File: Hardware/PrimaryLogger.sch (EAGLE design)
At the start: 72 parts, among them J1 CONN_42.54_SCREW, J2 CONN_42.54_SCREW, J3 CONN_42.54_SCREW, J4 CONN_42.54_SCREW, J5 CONN_32.54_SCREW, Q1 DMG3404, Q2 DMG3404, U1 MIC2005, U2 MIC2005, U25 SN74AUP3G34DCU, U3 TPL5010DDC, U4 TXS0102DCU, U5 SN74LVC1G3157SC70, U6 TCS3400, U7 SHTC3DFN, U8 MCP23008QFN, U9 MCP7940SOIC

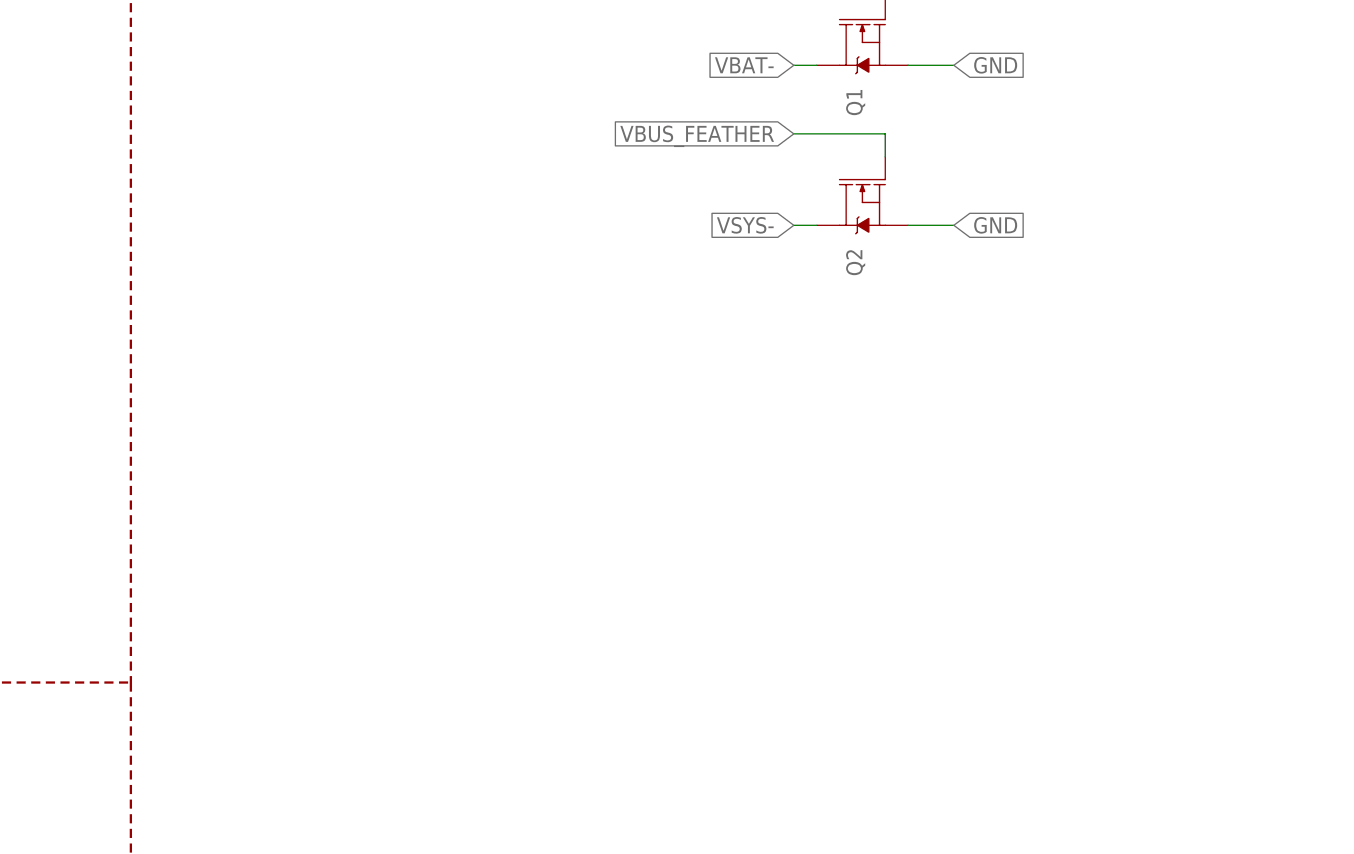
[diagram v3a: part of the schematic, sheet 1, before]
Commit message: Added LED support for v0.3
Schematic capture and preliminary layout of LED indicator
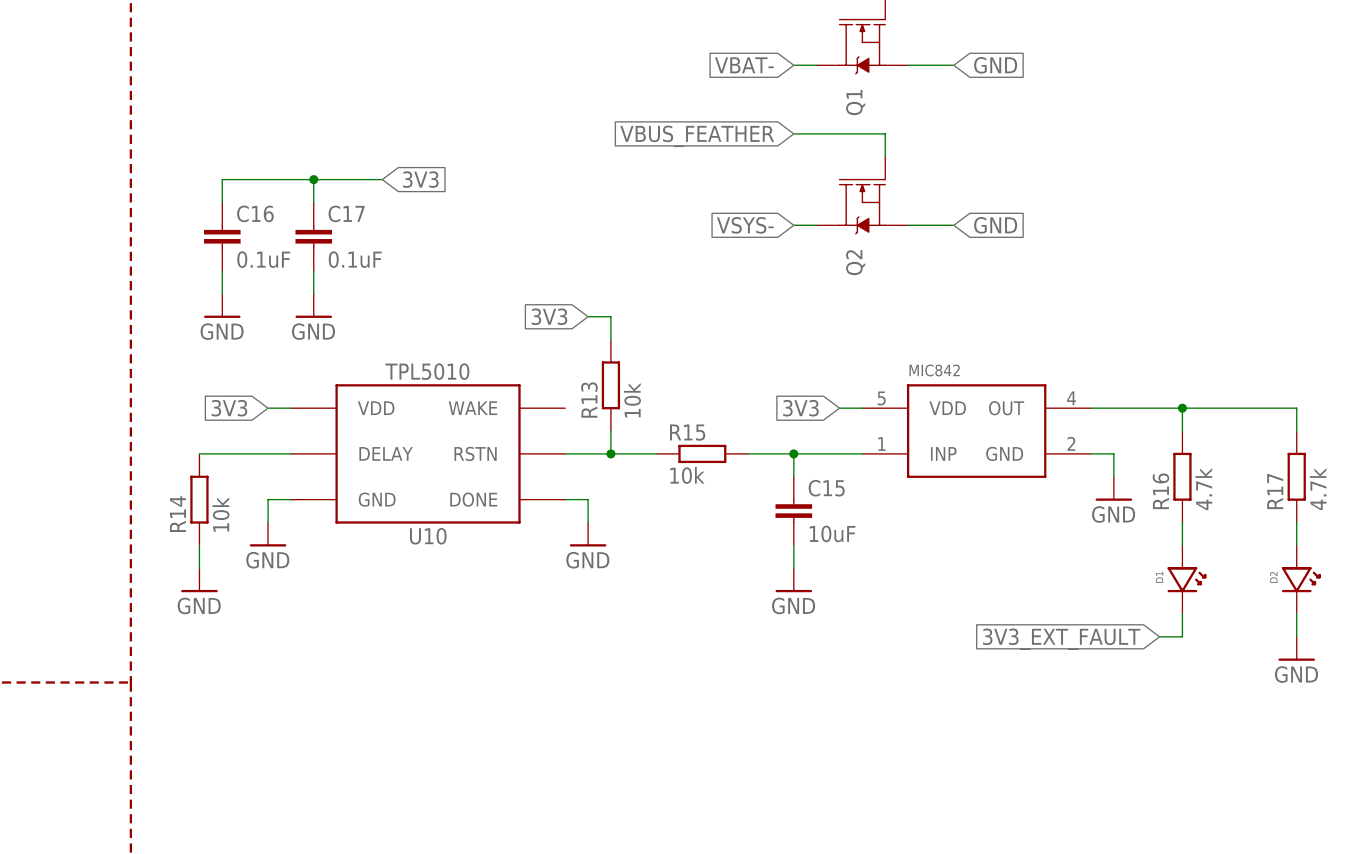
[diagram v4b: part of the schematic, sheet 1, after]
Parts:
- added C15: 10uF, bschulz_passives:C-EU10UFC0805
- added C16, C17: 0.1uF, bschulz_passives:C-EU0.1UFC0603
- added D1, D2: LED0603, bschulz:LED0603
- added R13, R14, R15: 10k, bschulz_passives:R-EU_10KR0603
- added R16, R17: 4.7k, bschulz_passives:R-EU_4.7KR0603
- added U10: TPL5010DDC, bschulz:TPL5010DDC
- added U11: MIC842, bschulz:MIC842
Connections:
- new net N$10: R16.2, R17.2, U11.OUT
- new net N$11: D1.ANODE, R16.1
- new net N$12: D2.ANODE, R17.1
- new net N$7: R14.2, U10.DELAY
- new net N$8: C15.1, R15.2, U11.INP
- new net N$9: R13.1, R15.1, U10.RSTN
- net 3V3: now also C16.1, C17.1, R13.2, U10.VDD, U11.VDD
- net 3V3_EXT_FAULT: now also D1.CATHODE
- net GND: now also C15.2, C16.2, C17.2, D2.CATHODE, R14.1, U10.DONE, U10.GND, U11.GND

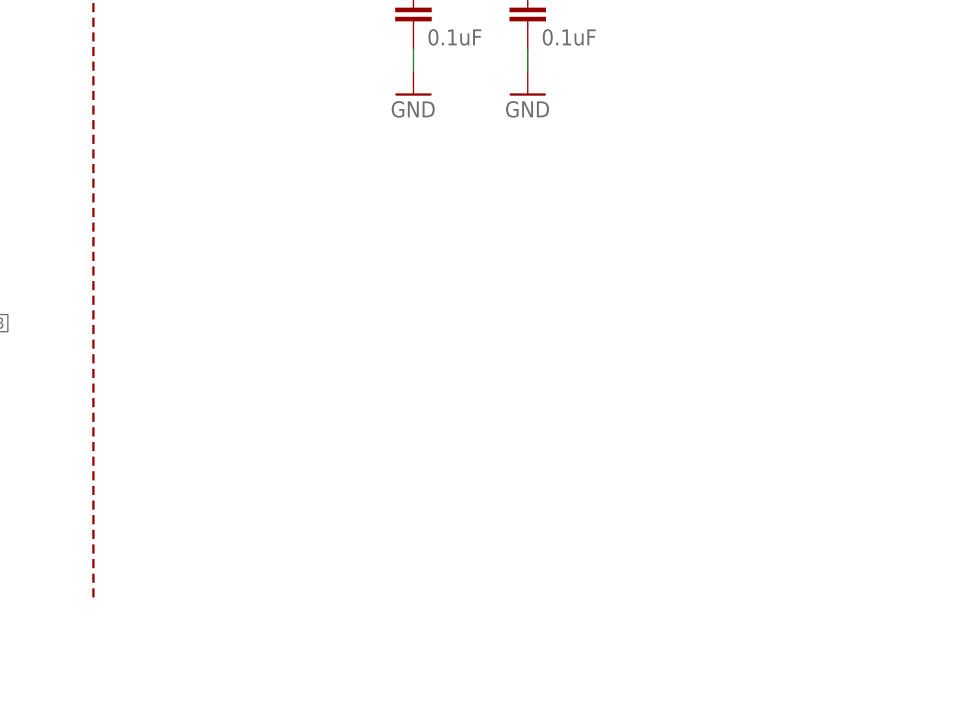
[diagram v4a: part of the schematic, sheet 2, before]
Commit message: Updated IO expander to SSOP package
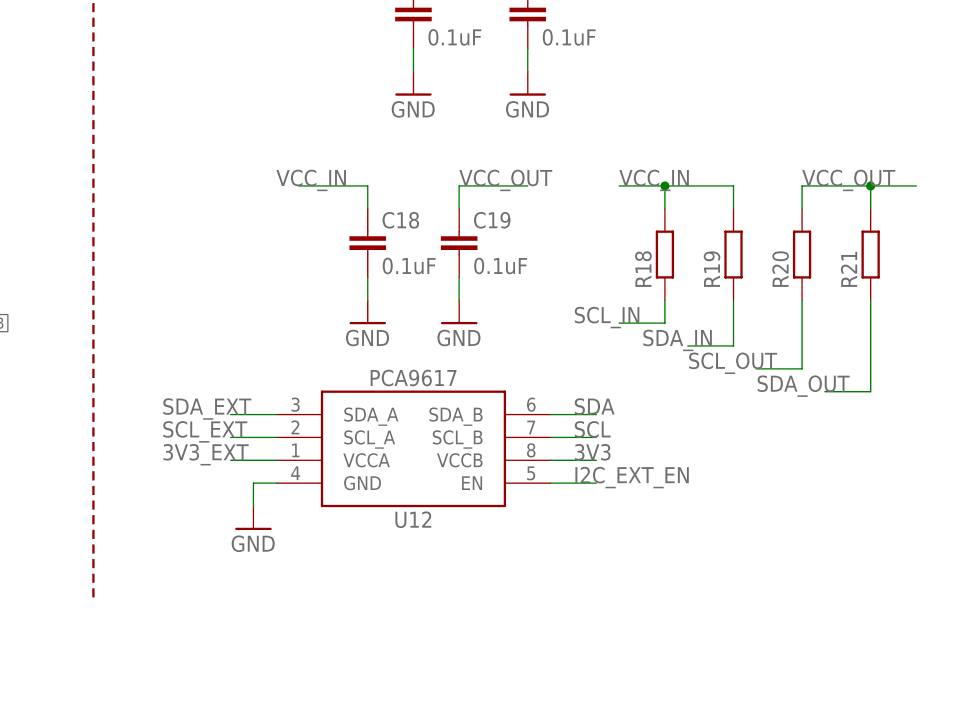
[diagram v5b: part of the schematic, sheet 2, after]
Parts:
- added C18, C19: 0.1uF, bschulz_passives:C-EU0.1UFC0603
- added R18, R19, R20, R21: (no value), bschulz_passives:R-EU_4.7KR0603
- added U12: PCA9617TSSOP8, bschulz:PCA9617TSSOP8
- added U13: MCP23008SSOP, bschulz:MCP23008SSOP
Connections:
- new net SCL_IN: R18.1
- new net SCL_OUT: R20.1
- new net SDA_IN: R19.1
- new net SDA_OUT: R21.1
- new net VCC_IN: C18.1, R18.2, R19.2
- new net VCC_OUT: C19.1, R20.2, R21.2
- net 3V3: now also U12.VCCB, U13.VDD
- net 3V3_EXT: now also U12.VCCA
- net 3V3_EXT_FAULT: now also U13.GP0
- net 3V3_SD_FAULT: now also U13.GP1
- net GND: now also C18.2, C19.2, U12.GND, U13.A0, U13.A1, U13.A2, U13.VSS
- net I2C_EXT_EN: now also U12.EN, U13.GP3
- net IO_EXP_INT: now also U13.INT
- net PAR_INT: now also U13.GP4
- net RST: now also U13.!RESET
- net SCL: now also U12.SCL_B, U13.SCL
- net SCL_EXT: now also U12.SCL_A
- net SDA: now also U12.SDA_B
- net SDA_EXT: now also U12.SDA_A
- net SDA_OB: now also U13.SDA
- net SD_CD: now also U13.GP2
- net WAKE: now also U13.GP5

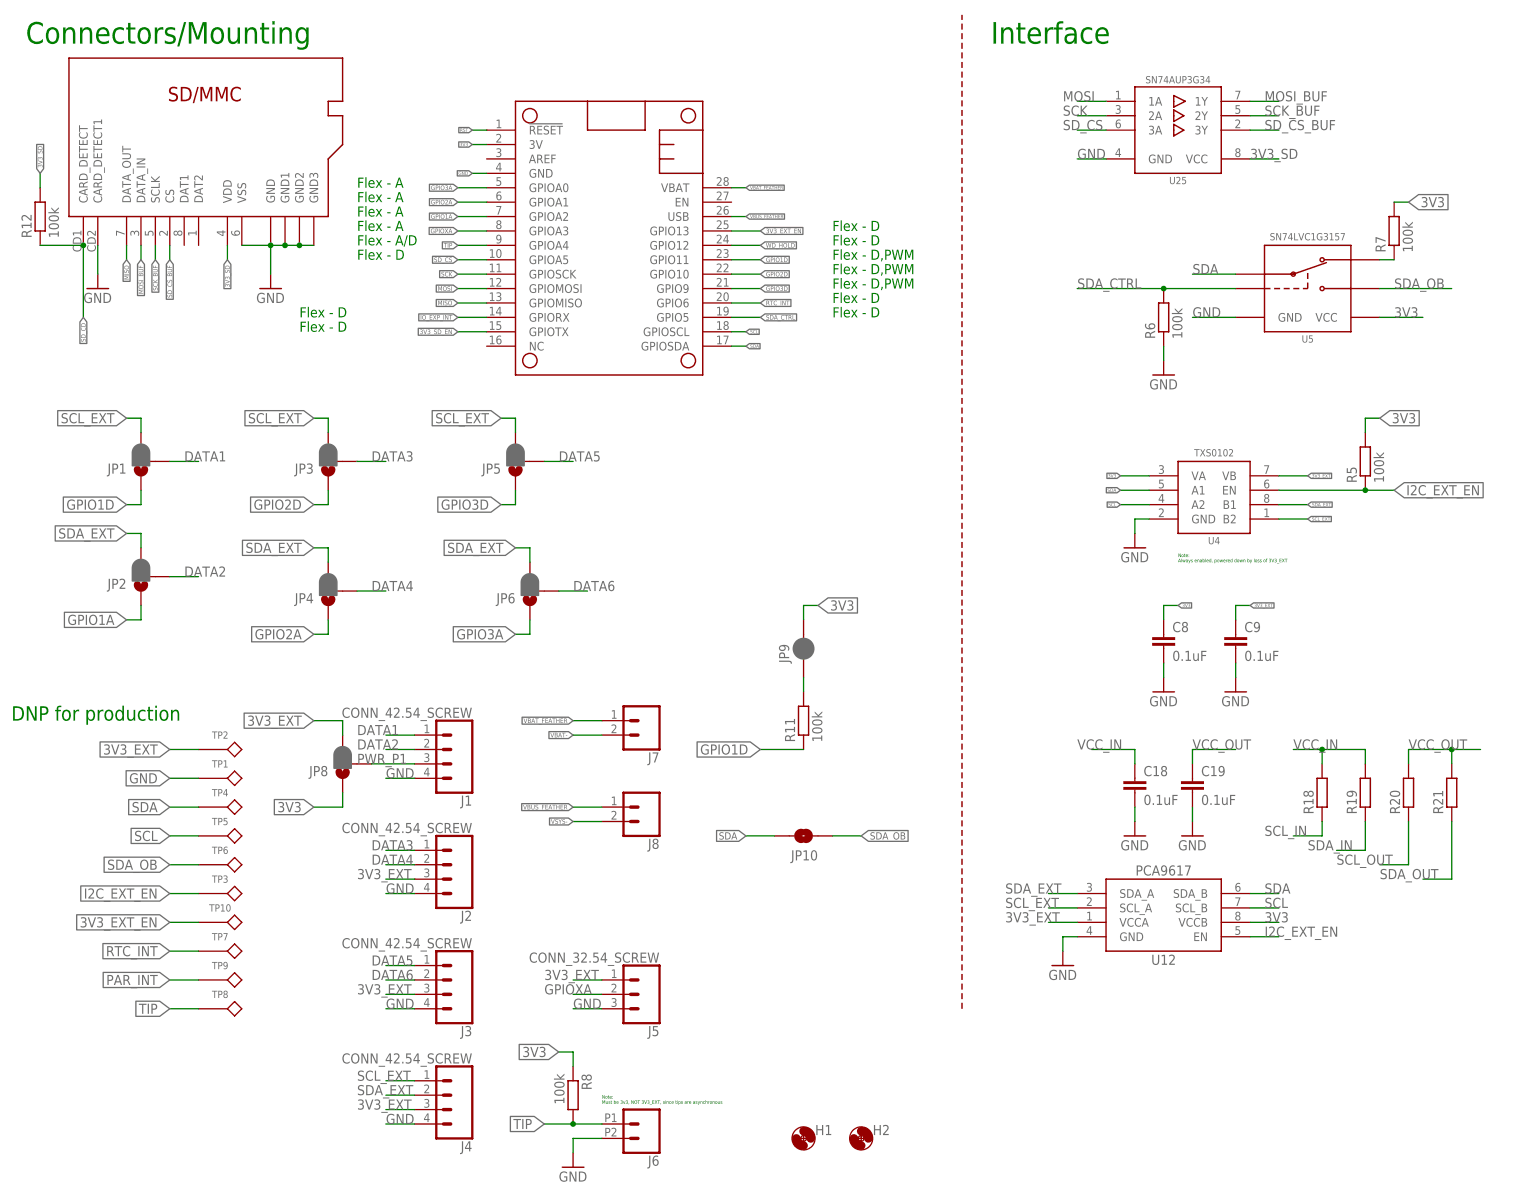
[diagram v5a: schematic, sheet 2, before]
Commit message: Added Niagara, jumpers, power connector
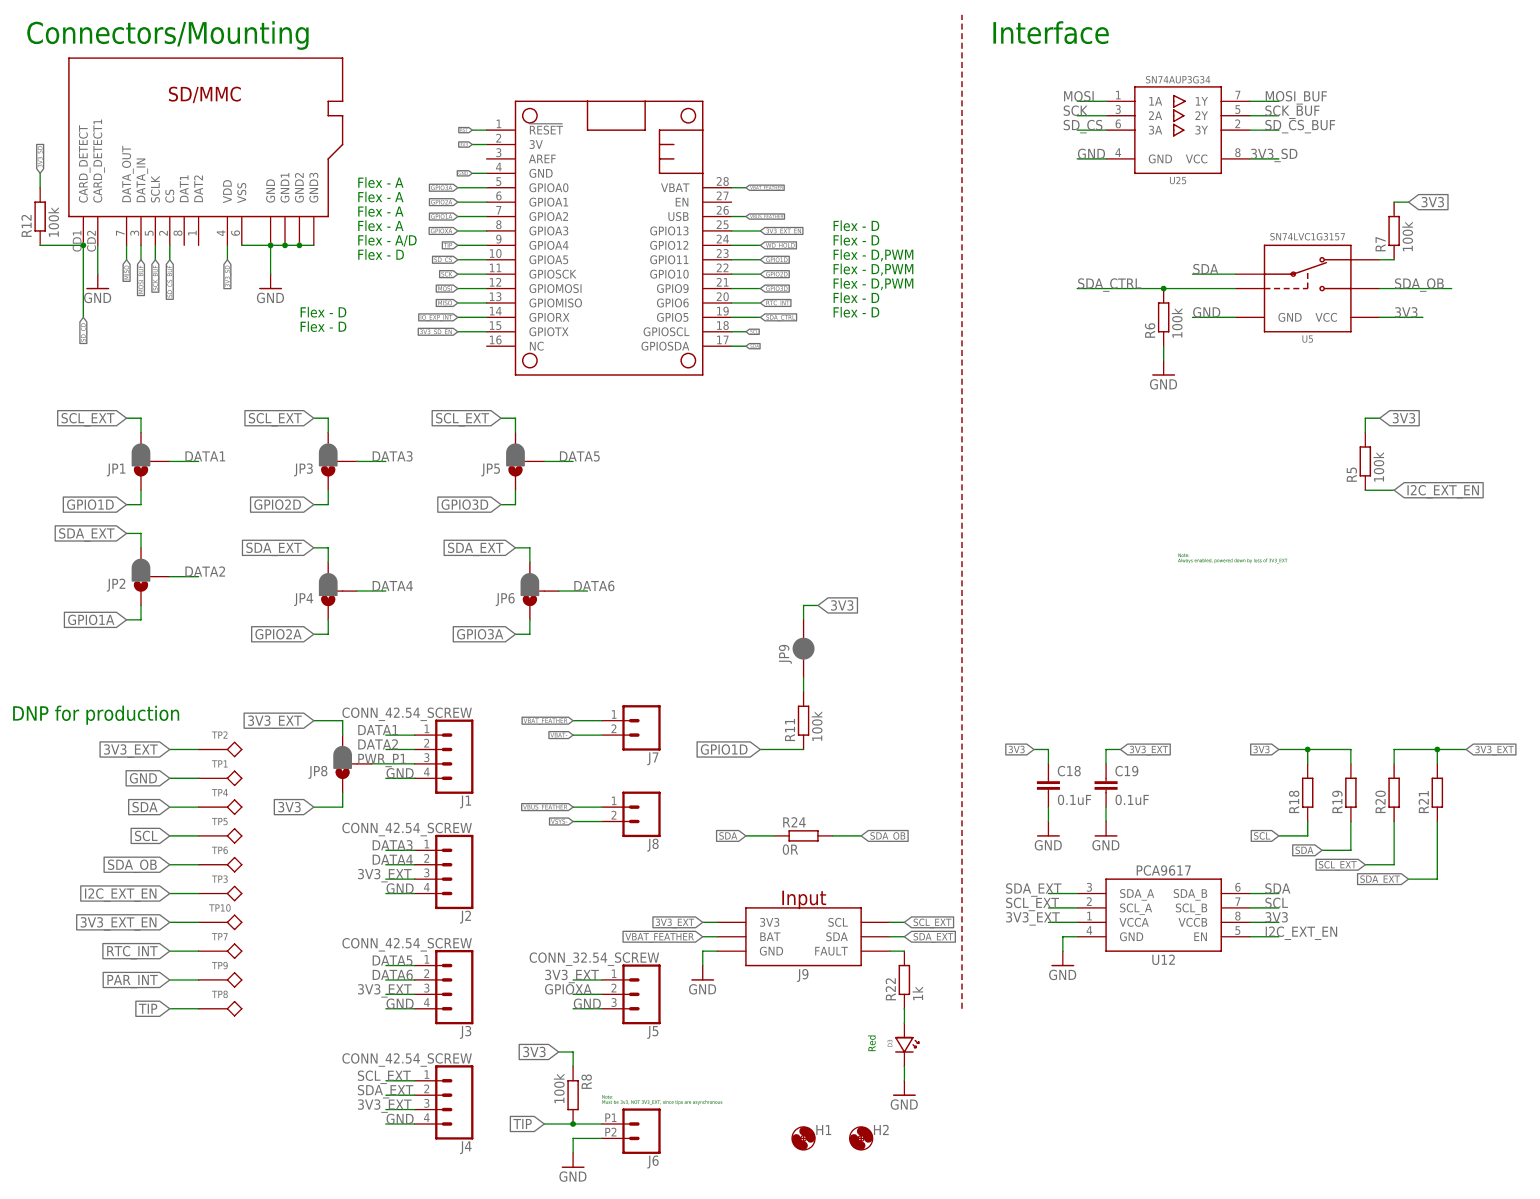
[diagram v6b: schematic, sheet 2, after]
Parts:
- removed C8, C9: 0.1uF, bschulz_passives:C-EU0.1UFC0603
- removed JP10: JUMPER-SMT_2_NO_SILK, bschulz:JUMPER-SMT_2_NO_SILK
- removed JP7: JUMPER-SMT_2_NC_PASTE_SILK, SparkFun-Jumpers:JUMPER-SMT_2_NC_PASTE_SILK
- removed U4: TXS0102DCU, bschulz:TXS0102DCU
- removed U8: MCP23008QFN, bschulz:MCP23008QFN
- added D3: LEDRED0603, bschulz:LEDRED0603
- added J9: GEMS_POWER_PLUGINPUT, bschulz:GEMS_POWER_PLUGINPUT
- added R22: 1k, bschulz_passives:R-EU_1KR0603
- added R23, R24: 0R, bschulz_passives:R-EU_R0603
- H1, H2: device bschulz:MOUNTING_HOLE4_NP -> bschulz:MOUNTING_HOLE2_NP
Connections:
- removed net SCL_IN: R18.1
- removed net SCL_OUT: R20.1
- removed net SDA_IN: R19.1
- removed net SDA_OUT: R21.1
- removed net VCC_IN: C18.1, R18.2, R19.2
- removed net VCC_OUT: C19.1, R20.2, R21.2
- new net N$13: J9.FAULT, R22.2
- new net N$14: D3.ANODE, R22.1
- net 3V3: now also C18.1, R18.2, R19.2, R23.2; no longer C8.1, JP7.2, U4.VA, U8.VDD
- net 3V3_EXT: now also C19.1, J9.3V3, R20.2, R21.2; no longer C9.1, U4.VB
- net 3V3_EXT_FAULT: no longer U8.GP0
- net 3V3_SD_FAULT: no longer U8.GP1
- net GND: now also D3.CATHODE, J9.GND; no longer C8.2, C9.2, U4.GND, U8.A0, U8.A1, U8.A2, U8.VSS
- net I2C_EXT_EN: no longer U4.EN, U8.GP3
- net IO_EXP_INT: no longer U8.INT
- net N$6: now also R23.1; no longer JP7.1
- net PAR_INT: no longer U8.GP4
- net RST: no longer U8.!RESET
- net SCL: now also R18.1; no longer U4.A2, U8.SCL
- net SCL_EXT: now also J9.SCL, R20.1; no longer U4.B2
- net SDA: now also R19.1, R24.1; no longer JP10.2, U4.A1
- net SDA_EXT: now also J9.SDA, R21.1; no longer U4.B1
- net SDA_OB: now also R24.2; no longer JP10.1, U8.SDA
- net SD_CD: no longer U8.GP2
- net VBAT_FEATHER: now also J9.BAT
- net WAKE: no longer U8.GP5
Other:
- note added: "Red"
- moved on the sheet: C18, C19, R18, R19, R20, R21
